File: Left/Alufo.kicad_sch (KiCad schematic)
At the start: 26 parts, among them J1 USB_C_Receptacle_USB2.0_16P_2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, J3 USB_C_Receptacle_USB2.0_16P_2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, SW10 BOOT, U1 CH552T, U3 USBLC6-2P6, U5 USBLC6-2P6

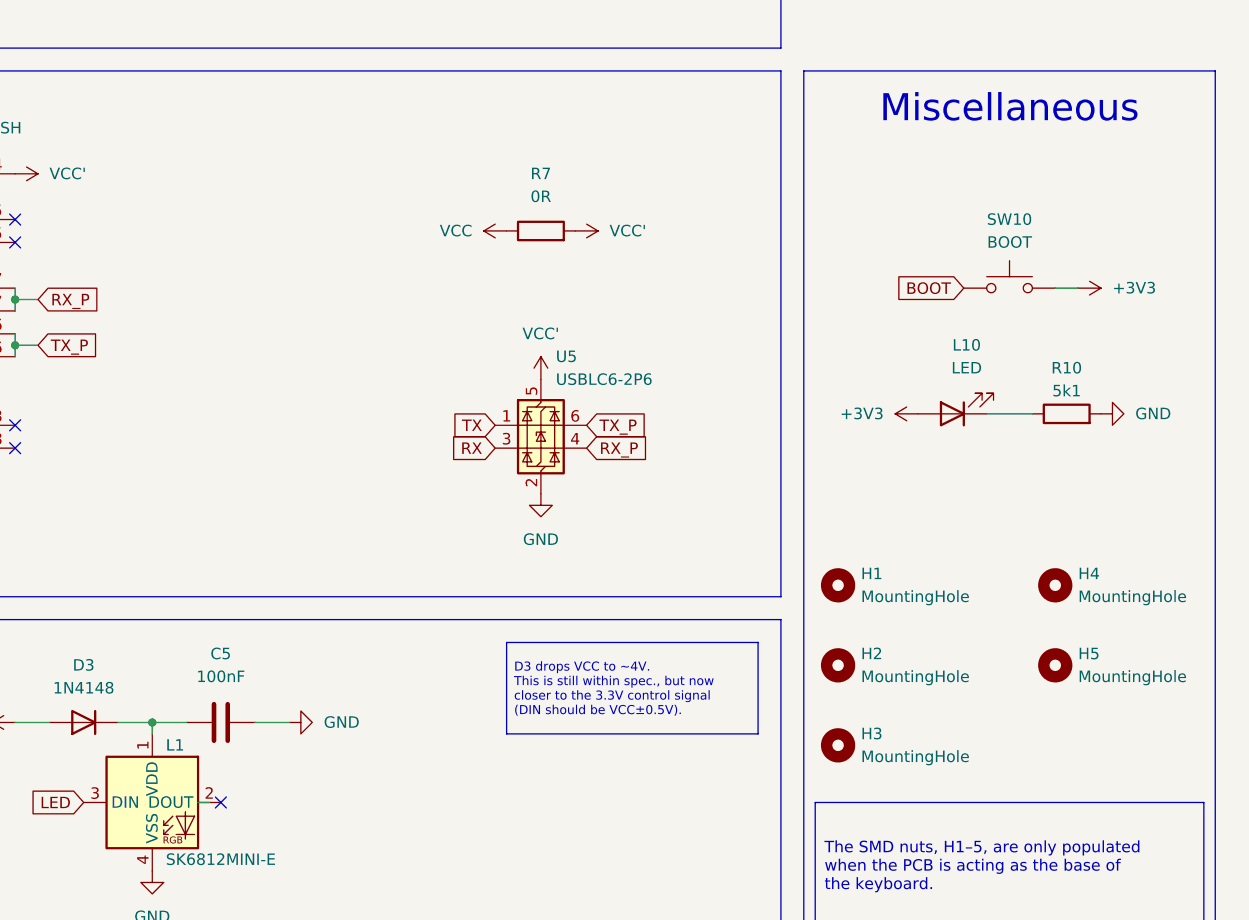
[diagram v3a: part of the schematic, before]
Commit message: Renumber previously common components
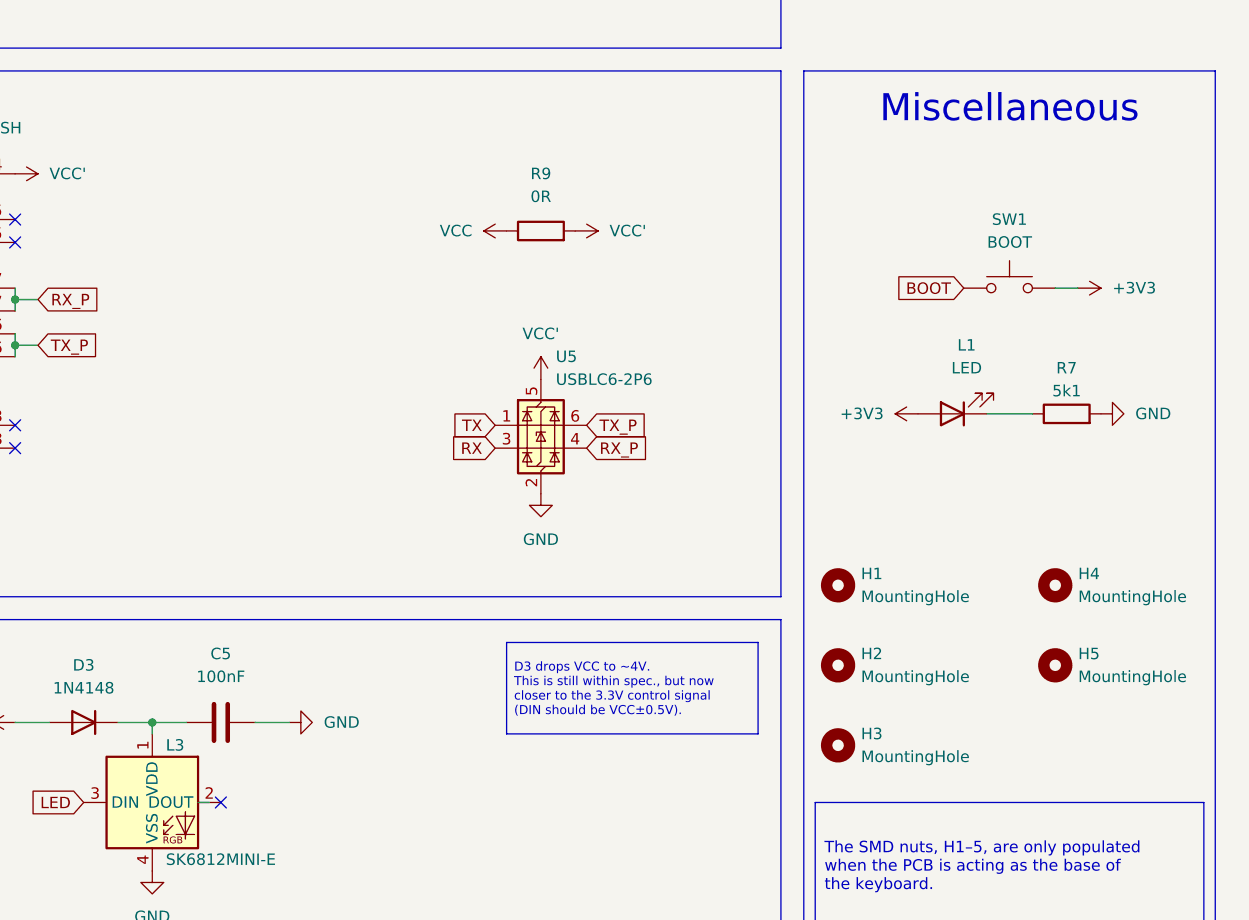
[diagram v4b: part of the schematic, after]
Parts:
- renumbered L10 to L1, L1 to L3, R10 to R7, R7 to R9, SW10 to SW1
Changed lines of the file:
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@@
 		(dnp no)
 		(fields_autoplaced yes)
-		(property "Reference" "L10"
+		(property "Reference" "L1"
 			(at 167.9575 170.18 0)
 			(effects
@@
 			(project ""
 				(path "/52f043ac-ccff-4c85-bc10-2db9d3c9e3f3"
-					(reference "L10")
+					(reference "L1")
 					(unit 1)
 				)
@@
 		(on_board yes)
 		(dnp no)
-		(property "Reference" "L1"
+		(property "Reference" "L3"
 			(at 80.01 214.63 0)
 			(effects
@@
 			(project ""
 				(path "/52f043ac-ccff-4c85-bc10-2db9d3c9e3f3"
-					(reference "L1")
+					(reference "L3")
 					(unit 1)
 				)
@@
 		(on_board yes)
 		(dnp no)
-		(property "Reference" "R10"
+		(property "Reference" "R7"
 			(at 179.07 172.72 90)
 			(effects
@@
 			(project "Alufo"
 				(path "/52f043ac-ccff-4c85-bc10-2db9d3c9e3f3"
-					(reference "R10")
+					(reference "R7")
 					(unit 1)
 				)
@@
 		(dnp no)
 		(fields_autoplaced yes)
-		(property "Reference" "R7"
+		(property "Reference" "R9"
 			(at 120.65 151.13 90)
 			(effects
@@
 			(project "Alufo"
 				(path "/52f043ac-ccff-4c85-bc10-2db9d3c9e3f3"
-					(reference "R7")
+					(reference "R9")
 					(unit 1)
 				)
@@
 		(dnp no)
 		(fields_autoplaced yes)
-		(property "Reference" "SW10"
+		(property "Reference" "SW1"
 			(at 172.72 156.21 0)
 			(effects
@@
 			(project "Alufo"
 				(path "/52f043ac-ccff-4c85-bc10-2db9d3c9e3f3"
-					(reference "SW10")
-					(unit 1)
-				)
+					(reference "SW1")
+					(unit 1)
+				)

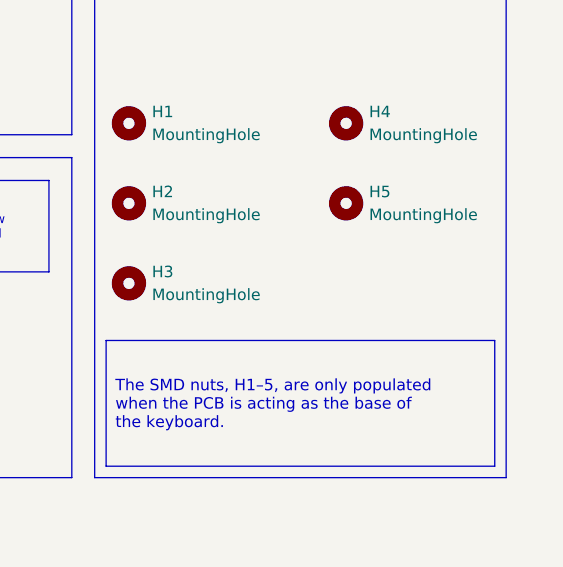
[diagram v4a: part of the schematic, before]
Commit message: Fix boot access hole location
Because the lefthand side PCB will become the base for the righthand board (and vice versa), and because the boot button is no longer centred, the hole in the base to allow access to the button must be on the opposite side of the centreline to that button. This means the access hole needs to be a separate component and the boot switch footprint no longer needs a central hole.
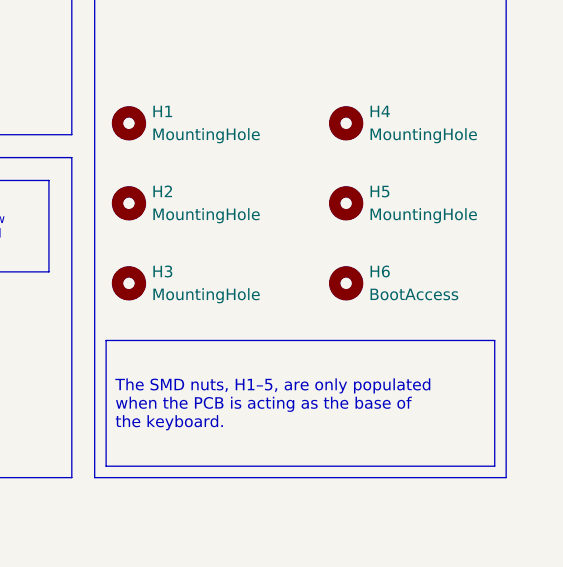
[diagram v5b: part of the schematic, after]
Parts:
- added H6: BootAccess, MountingHole:MountingHole_2.5mm, symbol Mechanical:MountingHole
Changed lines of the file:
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@@
+	(symbol
+		(lib_id "Mechanical:MountingHole")
+		(at 177.8 214.63 0)
+		(unit 1)
+		(exclude_from_sim yes)
+		(in_bom no)
+		(on_board yes)
+		(dnp no)
+		(fields_autoplaced yes)
+		(property "Reference" "H6"
+			(at 180.34 213.3599 0)
+			(effects
+				(font
+					(size 1.27 1.27)
+				)
+				(justify left)
+			)
+		)
+		(property "Value" "BootAccess"
+			(at 180.34 215.8999 0)
+			(effects
+				(font
+					(size 1.27 1.27)
+				)
+				(justify left)
+			)
+		)
+		(property "Footprint" "MountingHole:MountingHole_2.5mm"
+			(at 177.8 214.63 0)
+			(effects
+				(font
+					(size 1.27 1.27)
+				)
+				(hide yes)
+			)
+		)
+		(property "Datasheet" "~"
+			(at 177.8 214.63 0)
+			(effects
+				(font
+					(size 1.27 1.27)
+				)
+				(hide yes)
+			)
+		)
+		(property "Description" "Mounting Hole without connection"
+			(at 177.8 214.63 0)
+			(effects
+				(font
+					(size 1.27 1.27)
+				)
+				(hide yes)
+			)
+		)
+		(instances
+			(project "Alufo"
+				(path "/52f043ac-ccff-4c85-bc10-2db9d3c9e3f3"
+					(reference "H6")
+					(unit 1)
+				)
+			)
+		)
+	)
 	(symbol
 		(lib_id "Mechanical:MountingHole")
